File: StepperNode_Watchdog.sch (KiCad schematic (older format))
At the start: 5 parts

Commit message: Netlist top level
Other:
- note added: "Todo:\nJumper Pin to simulate failures."
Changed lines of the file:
@@
 Text Notes 8300 3100 0    60   ~ 0
 Active High when\nBoth watchdogs are good
+Text Notes 3800 4300 0    60   ~ 0
+Todo:\nJumper Pin to simulate failures.
 $EndSCHEMATC

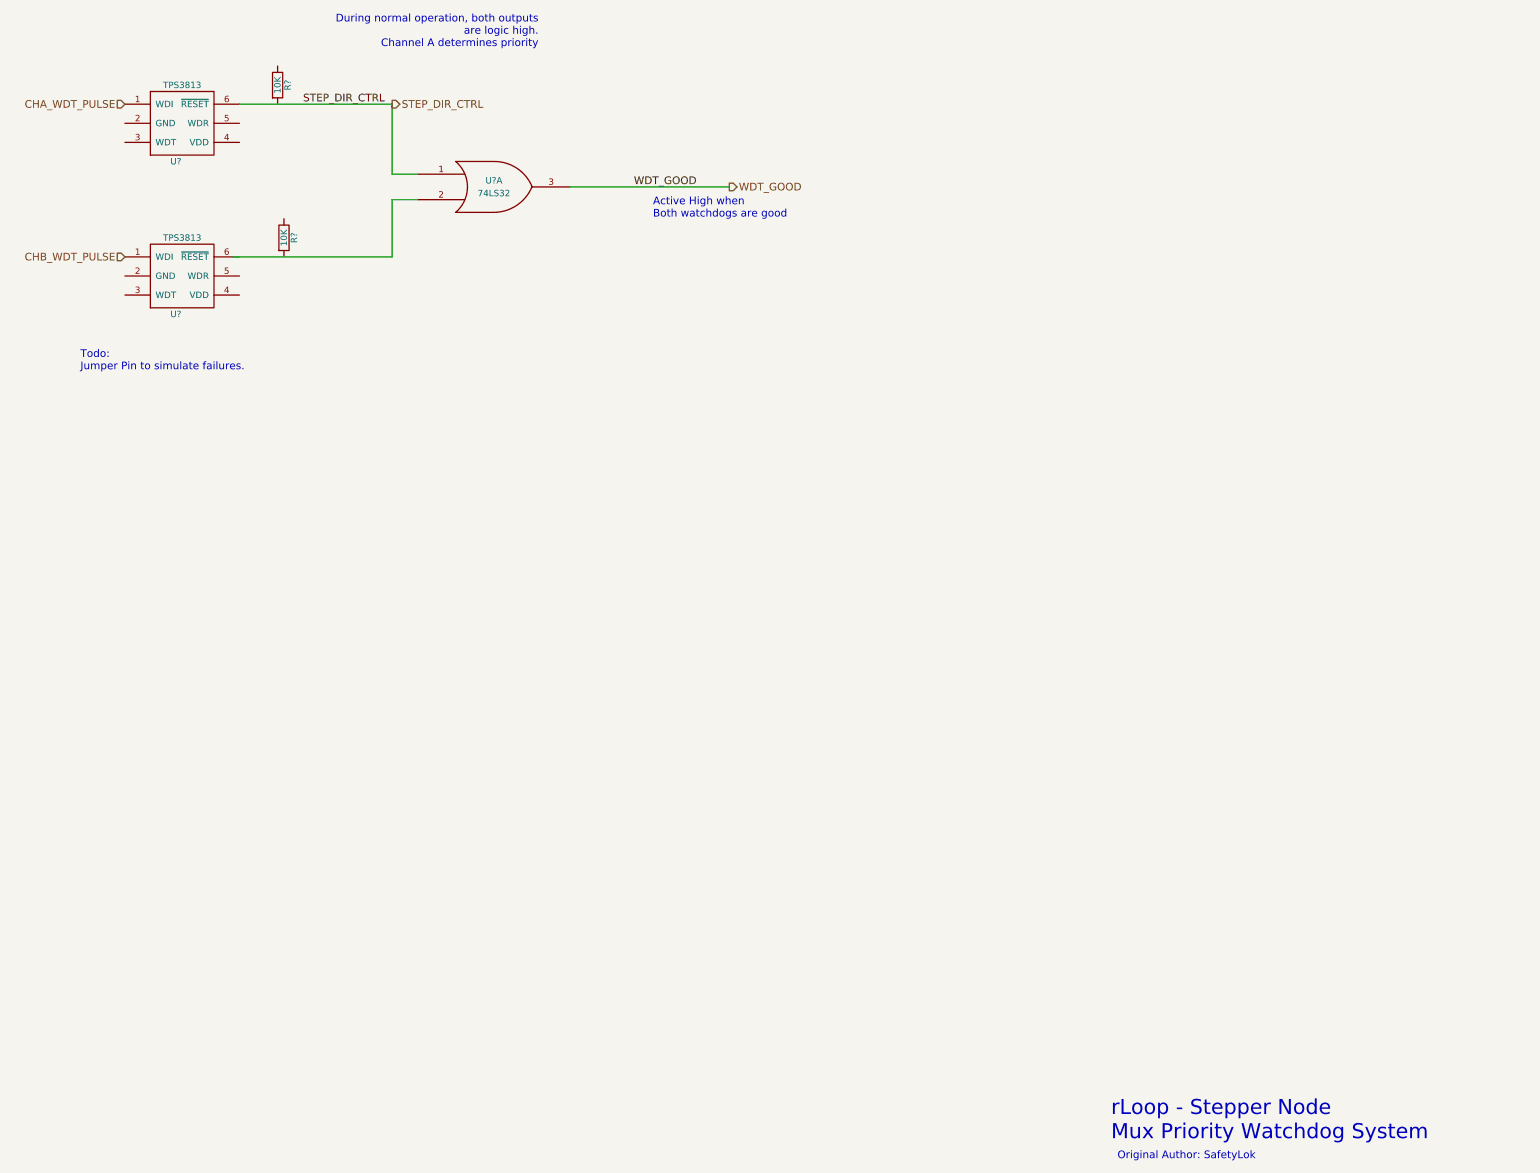
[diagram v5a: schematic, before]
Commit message: Updated node core connector pages and added interlocks.
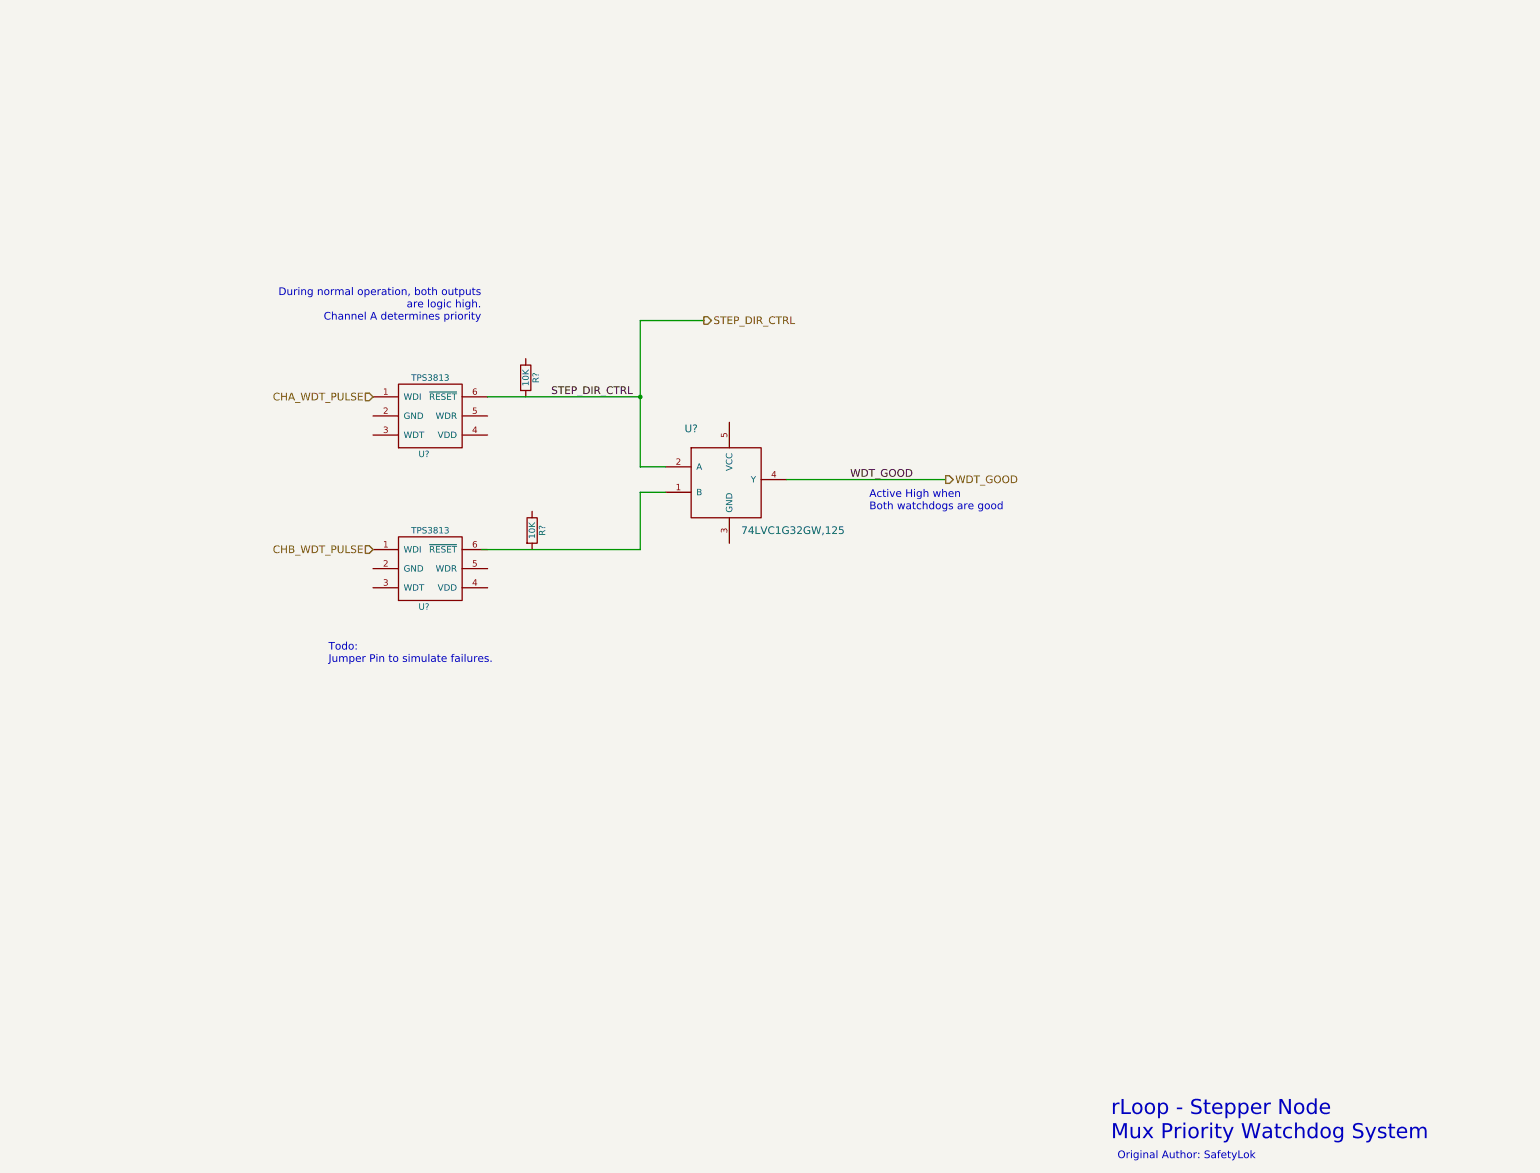
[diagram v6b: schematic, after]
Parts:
- removed U?: 74LS32, symbol 74LS32
- added U?: 74LVC1G32GW,125, symbol 74LVC1G32GW,125
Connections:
- wire segments 7 -> 8
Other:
- moved on the sheet: R?, U?
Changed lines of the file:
@@
 $Descr A3 16535 11693
 encoding utf-8
-Sheet 13 17
+Sheet 12 17
 Title "Watchdog"
 Date ""
@@
 Comment4 ""
 $EndDescr
-Text HLabel 6250 2200 2    60   Output ~ 0
+Text HLabel 8700 3900 2    60   Output ~ 0
 STEP_DIR_CTRL
 Text Notes 11900 10350 0    118  ~ 0
@@
 Text Notes 11950 10500 0    60   ~ 0
 Original Author: SafetyLok
-Text HLabel 4150 2200 0    60   Input ~ 0
+Text HLabel 6100 4500 0    60   Input ~ 0
 CHA_WDT_PULSE
-Text HLabel 4150 3400 0    60   Input ~ 0
+Text HLabel 6100 5700 0    60   Input ~ 0
 CHB_WDT_PULSE
 $Comp
 L TPS3813 U?
 U 1 1 5754A913
-P 4350 2600
-F 0 "U?" H 4550 2550 50  0000 C CNN
-F 1 "TPS3813" H 4600 3150 50  0000 C CNN
-F 2 "" H 4350 2600 50  0000 C CNN
-F 3 "" H 4350 2600 50  0000 C CNN
-	1    4350 2600
+P 6300 4900
+F 0 "U?" H 6500 4850 50  0000 C CNN
+F 1 "TPS3813" H 6550 5450 50  0000 C CNN
+F 2 "" H 6300 4900 50  0000 C CNN
+F 3 "" H 6300 4900 50  0000 C CNN
+	1    6300 4900
 	1    0    0    -1
 $EndComp
@@
 L TPS3813 U?
 U 1 1 5754A98A
-P 4350 3800
-F 0 "U?" H 4550 3750 50  0000 C CNN
-F 1 "TPS3813" H 4600 4350 50  0000 C CNN
-F 2 "" H 4350 3800 50  0000 C CNN
-F 3 "" H 4350 3800 50  0000 C CNN
-	1    4350 3800
-	1    0    0    -1
-$EndComp
-$Comp
-L 74LS32 U?
-U 1 1 5754AB6D
-P 7050 2850
-F 0 "U?" H 7050 2900 50  0000 C CNN
-F 1 "74LS32" H 7050 2800 50  0000 C CNN
-F 2 "" H 7050 2850 50  0000 C CNN
-F 3 "" H 7050 2850 50  0000 C CNN
-	1    7050 2850
+P 6300 6100
+F 0 "U?" H 6500 6050 50  0000 C CNN
+F 1 "TPS3813" H 6550 6650 50  0000 C CNN
+F 2 "" H 6300 6100 50  0000 C CNN
+F 3 "" H 6300 6100 50  0000 C CNN
+	1    6300 6100
 	1    0    0    -1
 $EndComp
 Wire Wire Line
-	5050 2200 6250 2200
+	7000 4500 8200 4500
 Wire Wire Line
-	6250 2200 6250 2750
+	8200 3900 8200 5050
 Wire Wire Line
-	6250 2750 6450 2750
+	8200 5050 8400 5050
 Wire Wire Line
-	5000 3400 6250 3400
+	6950 5700 8200 5700
 Wire Wire Line
-	6250 3400 6250 2950
+	8200 5700 8200 5250
 Wire Wire Line
-	6250 2950 6450 2950
-Text Notes 7400 1760 2    60   ~ 0
+	8200 5250 8400 5250
+Text Notes 6950 3910 2    60   ~ 0
 During normal operation, both outputs\nare logic high.\nChannel A determines priority
 $Comp
 L R R?
 U 1 1 5754AC39
-P 5350 2050
-F 0 "R?" V 5430 2050 50  0000 C CNN
-F 1 "10K" V 5350 2050 50  0000 C CNN
-F 2 "" V 5280 2050 50  0000 C CNN
-F 3 "" H 5350 2050 50  0000 C CNN
-	1    5350 2050
+P 7300 4350
+F 0 "R?" V 7380 4350 50  0000 C CNN
+F 1 "10K" V 7300 4350 50  0000 C CNN
+F 2 "" V 7230 4350 50  0000 C CNN
+F 3 "" H 7300 4350 50  0000 C CNN
+	1    7300 4350
 	1    0    0    -1
 $EndComp
@@
 L R R?
 U 1 1 5754ACDE
-P 5400 3250
-F 0 "R?" V 5480 3250 50  0000 C CNN
-F 1 "10K" V 5400 3250 50  0000 C CNN
-F 2 "" V 5330 3250 50  0000 C CNN
-F 3 "" H 5400 3250 50  0000 C CNN
-	1    5400 3250
+P 7350 5550
+F 0 "R?" V 7430 5550 50  0000 C CNN
+F 1 "10K" V 7350 5550 50  0000 C CNN
+F 2 "" V 7280 5550 50  0000 C CNN
+F 3 "" H 7350 5550 50  0000 C CNN
+	1    7350 5550
 	1    0    0    -1
 $EndComp
-Text Label 5550 2200 0    60   ~ 0
+Text Label 7500 4500 0    60   ~ 0
 STEP_DIR_CTRL
 Wire Wire Line
-	7650 2850 8900 2850
-Text HLabel 8900 2850 2    60   Output ~ 0
+	9350 5150 10600 5150
+Text HLabel 10600 5150 2    60   Output ~ 0
 WDT_GOOD
-Text Label 8150 2850 0    60   ~ 0
+Text Label 9850 5150 0    60   ~ 0
 WDT_GOOD
-Text Notes 8300 3100 0    60   ~ 0
+Text Notes 10000 5400 0    60   ~ 0
 Active High when\nBoth watchdogs are good
-Text Notes 3800 4300 0    60   ~ 0
+Text Notes 5750 6600 0    60   ~ 0
 Todo:\nJumper Pin to simulate failures.
+$Comp
+L 74LVC1G32GW,125 U?
+U 1 1 575DE6F6
+P 8600 4900
+F 0 "U?" H 8600 5050 60  0000 C CNN
+F 1 "74LVC1G32GW,125" H 9400 4250 60  0000 C CNN
+F 2 "" H 8600 4900 60  0000 C CNN
+F 3 "" H 8600 4900 60  0000 C CNN
+	1    8600 4900
+	1    0    0    -1
+$EndComp
+Wire Wire Line
+	8700 3900 8200 3900
+Connection ~ 8200 4500
 $EndSCHEMATC
